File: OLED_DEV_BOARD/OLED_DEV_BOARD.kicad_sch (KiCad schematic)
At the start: 1 part

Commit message: Added some parts
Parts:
- added U?: NCP1117-3.3_TO252, Package_TO_SOT_SMD:TO-252-2, symbol Regulator_Linear:NCP1117-3.3_TO252
- added U?: IS66WVS1M8BLL-104NLI, symbol OLED:IS66WVS1M8BLL-104NLI
- added U?: W25Q32JVSS, Package_SO:SOIC-8_5.23x5.23mm_P1.27mm, symbol Memory_Flash:W25Q32JVSS
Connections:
- net +3V3: now also U?.8 (VCC), U?.8 (VDD)
- net GND: now also U?.4 (GND), U?.4 (VSS)
- new net FLASH_CLK: U?.6 (CLK)
- new net FLASH_CSb: U?.1 (~{CS})
- new net FLASH_D0: U?.5 (DI(IO0))
- new net FLASH_D1: U?.2 (DO(IO1))
- new net FLASH_D2: U?.3 (IO2)
- new net FLASH_D3: U?.7 (IO3)
- new net PSRAM_CLK: U?.6 (CLK)
- new net PSRAM_CSb: U?.1 (CE#)
- new net PSRAM_D0: U?.5 (SI/SIO0)
- new net PSRAM_D1: U?.2 (SO/SIO1)
- new net PSRAM_D2: U?.3 (SIO2)
- new net PSRAM_D3: U?.7 (SIO3)

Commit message: Added switches
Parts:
- added C?: 100uF, symbol Device:C_Polarized
- added C? (x2): 10uF, symbol Device:C_Polarized
- added C? (x2): 100nF, symbol Device:C
- added C? (x2): 1uF, symbol Device:C
- added C?: 1nF, symbol Device:C
- added D?: 1N4004, Diode_THT:D_DO-41_SOD81_P10.16mm_Horizontal, symbol Diode:1N4004
- added J?: Conn_02x20_Odd_Even, symbol Connector_Generic:Conn_02x20_Odd_Even
- added J?: AudioJack3_Ground, Connector_Audio:Jack_3.5mm_CUI_SJ-3523-SMT_Horizontal, symbol Connector:AudioJack3_Ground
- added J?: Barrel_Jack, symbol Connector:Barrel_Jack
- added R? (x9): 5k6, symbol Device:R
- added SW? (x6): SW_MEC_5E, symbol Switch:SW_MEC_5E
- added SW?: SW_DIP_x02, symbol Switch:SW_DIP_x02
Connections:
- net +3V3: now also U?.2 (VO), C?.1, C?.1, C?.1, C?.1, C?.1, C?.1, D?.2 (A), SW?.3, SW?.3 (K), SW?.3 (K), SW?.3 (K), SW?.3 (K), SW?.3 (K), SW?.3 (K), SW?.4, SW?.4 (A), SW?.4 (A), SW?.4 (A), SW?.4 (A), SW?.4 (A), SW?.4 (A)
- net GND: now also U?.1 (GND), C?.2, C?.2, C?.2, C?.2, C?.2, C?.2, C?.2, C?.2, J?.1 (Pin_1), J?.2, J?.2 (Pin_2), J?.39 (Pin_39), J?.40 (Pin_40), J?.G, J?.S, R?.1, R?.1, R?.1, R?.1, R?.1, R?.1, R?.1, R?.2
- net at U?.3 (VI): now also C?.1, D?.1 (K), J?.1
- new net: R?.2, SW?.1, SW?.2 (x5)
- new net: R?.1, SW?.1, SW?.2
- new net: C?.1, J?.R, J?.T, R?.2
- new net: R?.2, SW?.1
- new net: R?.2, SW?.2
- new net PWM: R?.1
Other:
- moved on the sheet: U?

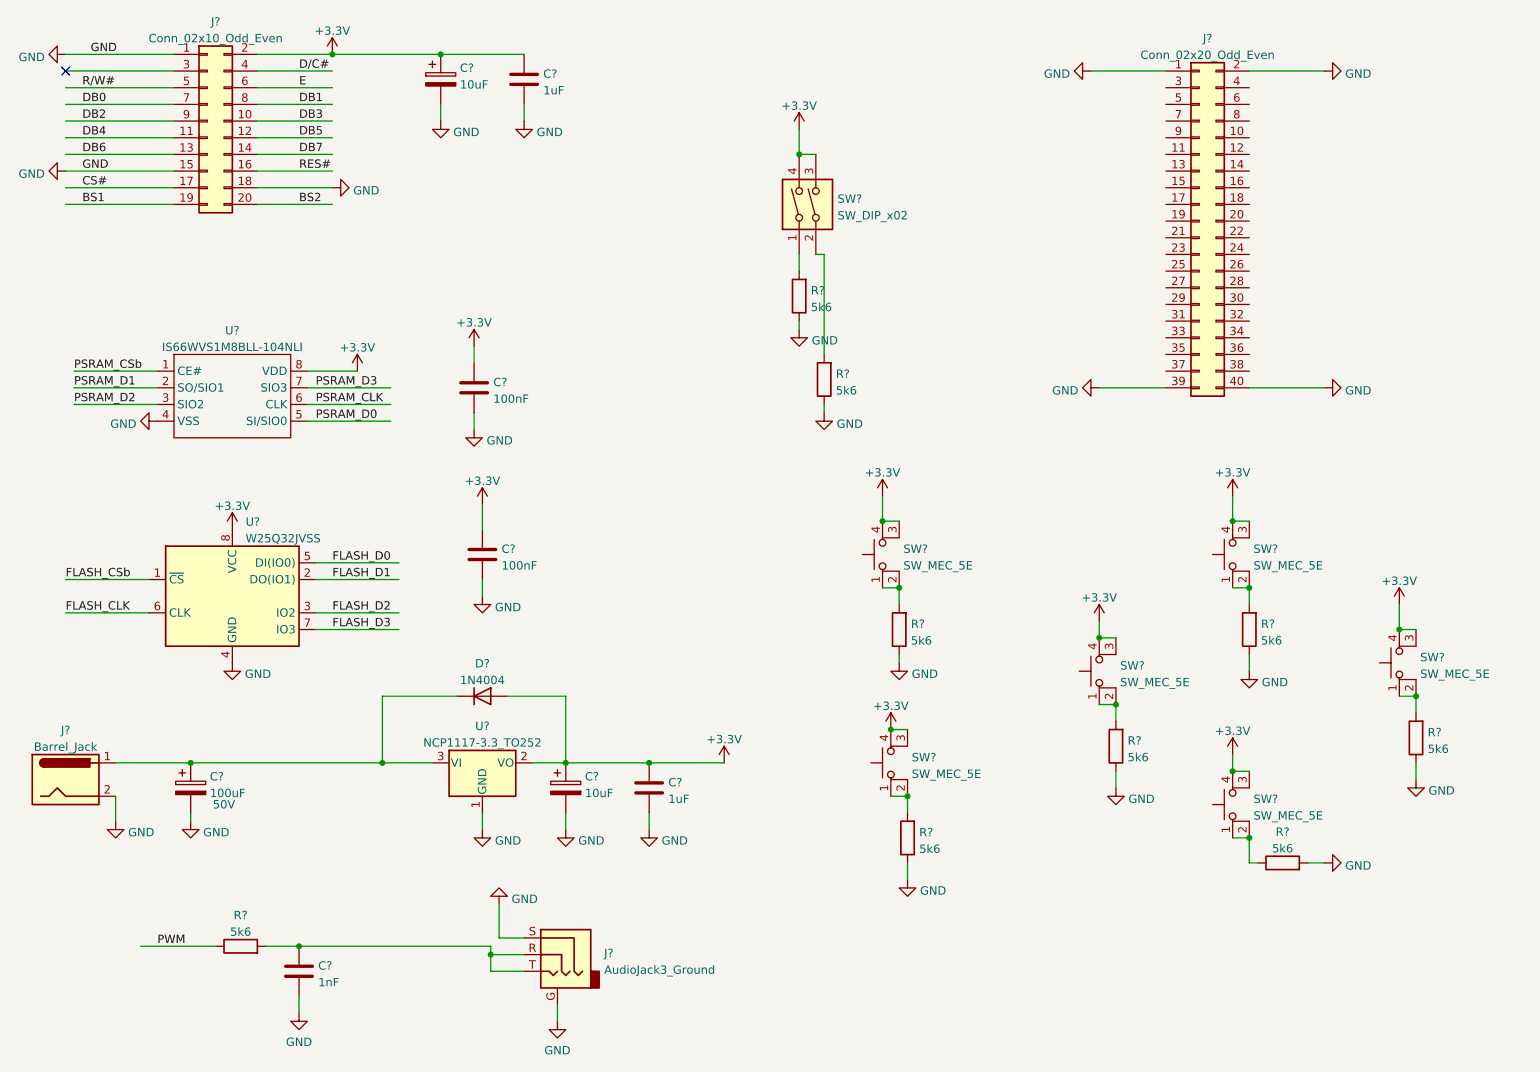
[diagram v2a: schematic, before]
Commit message: Added signals to connector
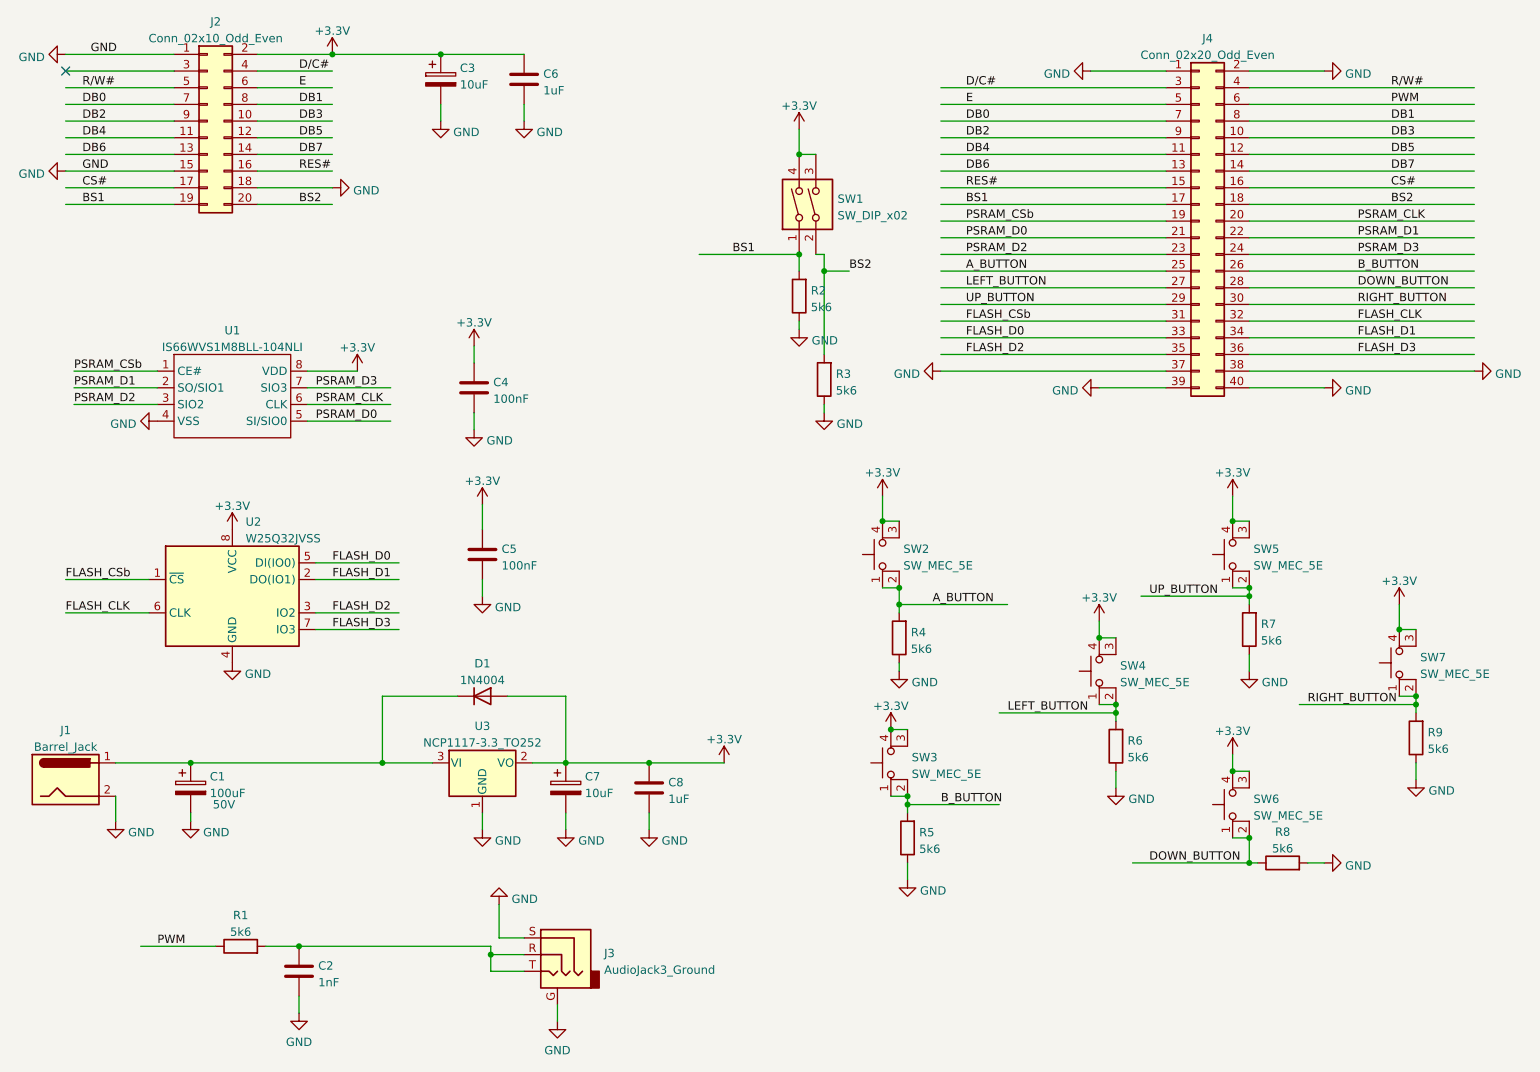
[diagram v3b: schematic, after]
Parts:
- gave numbers to parts that had none: 32
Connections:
- net BS1: now also J4.17 (Pin_17), R2.2, SW1.1
- net BS2: now also J4.18 (Pin_18), R3.2, SW1.2
- net CS#: now also J4.16 (Pin_16)
- net DB0: now also J4.7 (Pin_7)
- net DB1: now also J4.8 (Pin_8)
- net DB2: now also J4.9 (Pin_9)
- net DB3: now also J4.10 (Pin_10)
- net DB4: now also J4.11 (Pin_11)
- net DB5: now also J4.12 (Pin_12)
- net DB6: now also J4.13 (Pin_13)
- net DB7: now also J4.14 (Pin_14)
- net D/C#: now also J4.3 (Pin_3)
- net E: now also J4.5 (Pin_5)
- net FLASH_CLK: now also J4.32 (Pin_32)
- net FLASH_CSb: now also J4.31 (Pin_31)
- net FLASH_D0: now also J4.33 (Pin_33)
- net FLASH_D1: now also J4.34 (Pin_34)
- net FLASH_D2: now also J4.35 (Pin_35)
- net FLASH_D3: now also J4.36 (Pin_36)
- net GND: now also J4.37 (Pin_37), J4.38 (Pin_38)
- net PSRAM_CLK: now also J4.20 (Pin_20)
- net PSRAM_CSb: now also J4.19 (Pin_19)
- net PSRAM_D0: now also J4.21 (Pin_21)
- net PSRAM_D1: now also J4.22 (Pin_22)
- net PSRAM_D2: now also J4.23 (Pin_23)
- net PSRAM_D3: now also J4.24 (Pin_24)
- net PWM: now also J4.6 (Pin_6)
- net RES#: now also J4.15 (Pin_15)
- net R/W#: now also J4.4 (Pin_4)
- net B_BUTTON: now reaches R5.2, SW3.1, SW3.2
- net B_BUTTON: now also J4.26 (Pin_26)
- net RIGHT_BUTTON: now reaches R9.2, SW7.1, SW7.2
- net RIGHT_BUTTON: now also J4.30 (Pin_30)
- net UP_BUTTON: now reaches R7.2, SW5.1, SW5.2
- net UP_BUTTON: now also J4.29 (Pin_29)
- net LEFT_BUTTON: now reaches R6.2, SW4.1, SW4.2
- net LEFT_BUTTON: now also J4.27 (Pin_27)
- net A_BUTTON: now reaches J4.25 (Pin_25)
- net A_BUTTON: now also R4.2, SW2.1, SW2.2
- net DOWN_BUTTON: now reaches J4.28 (Pin_28)
- net DOWN_BUTTON: now also R8.1, SW6.1, SW6.2
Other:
- moved on the sheet: R4

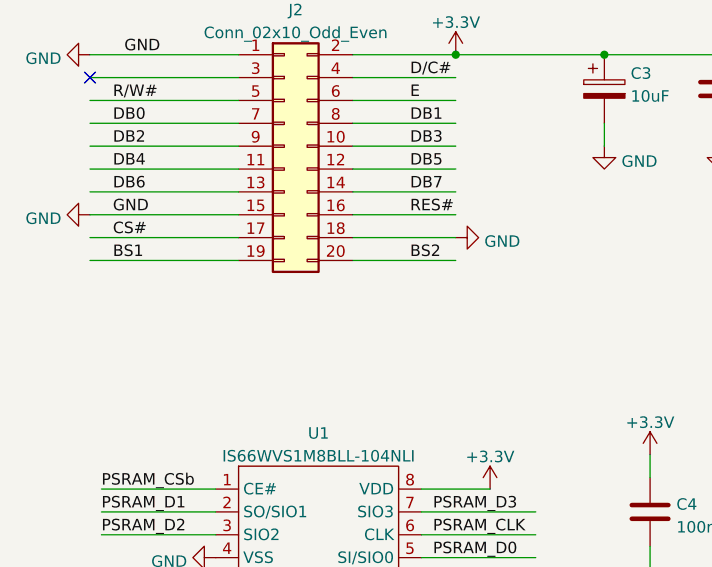
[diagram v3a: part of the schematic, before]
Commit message: Added part number to header
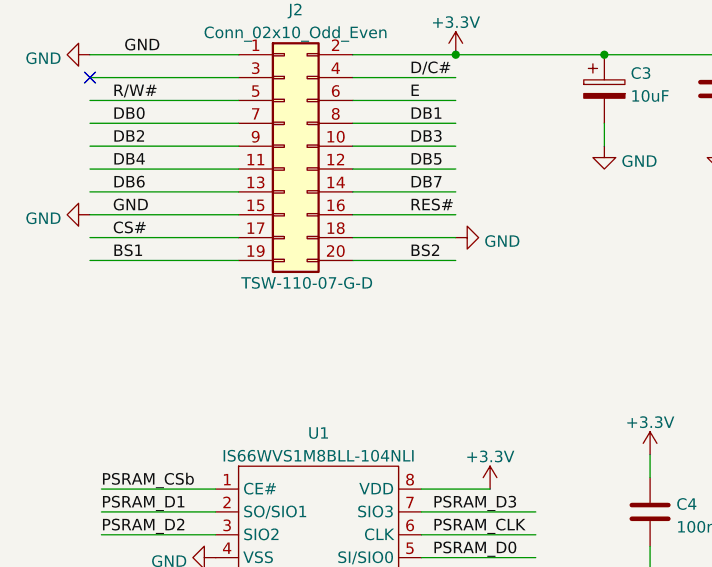
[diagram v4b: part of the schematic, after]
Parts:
- J2: Manufacturer Part Number (none) -> TSW-110-07-G-D; Mouser Part Number (none) -> 200-TSW11007GD
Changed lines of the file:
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@@
   )
   (symbol (lib_id "Connector_Generic:Conn_02x10_Odd_Even") (at 48.26 45.72 0) (unit 1)
-    (in_bom yes) (on_board yes) (fields_autoplaced)
+    (in_bom yes) (on_board yes)
     (property "Reference" "J2" (id 0) (at 49.53 30.5902 0))
     (property "Value" "Conn_02x10_Odd_Even" (id 1) (at 49.53 33.1271 0))
@@
       (effects (font (size 1.27 1.27)) hide)
     )
+    (property "Mouser Part Number" "200-TSW11007GD " (id 4) (at 48.26 45.72 0)
+      (effects (font (size 1.27 1.27)) hide)
+    )
+    (property "Manufacturer Part Number" "TSW-110-07-G-D " (id 5) (at 50.8 60.96 0))
     (pin "1")
     (pin "10")

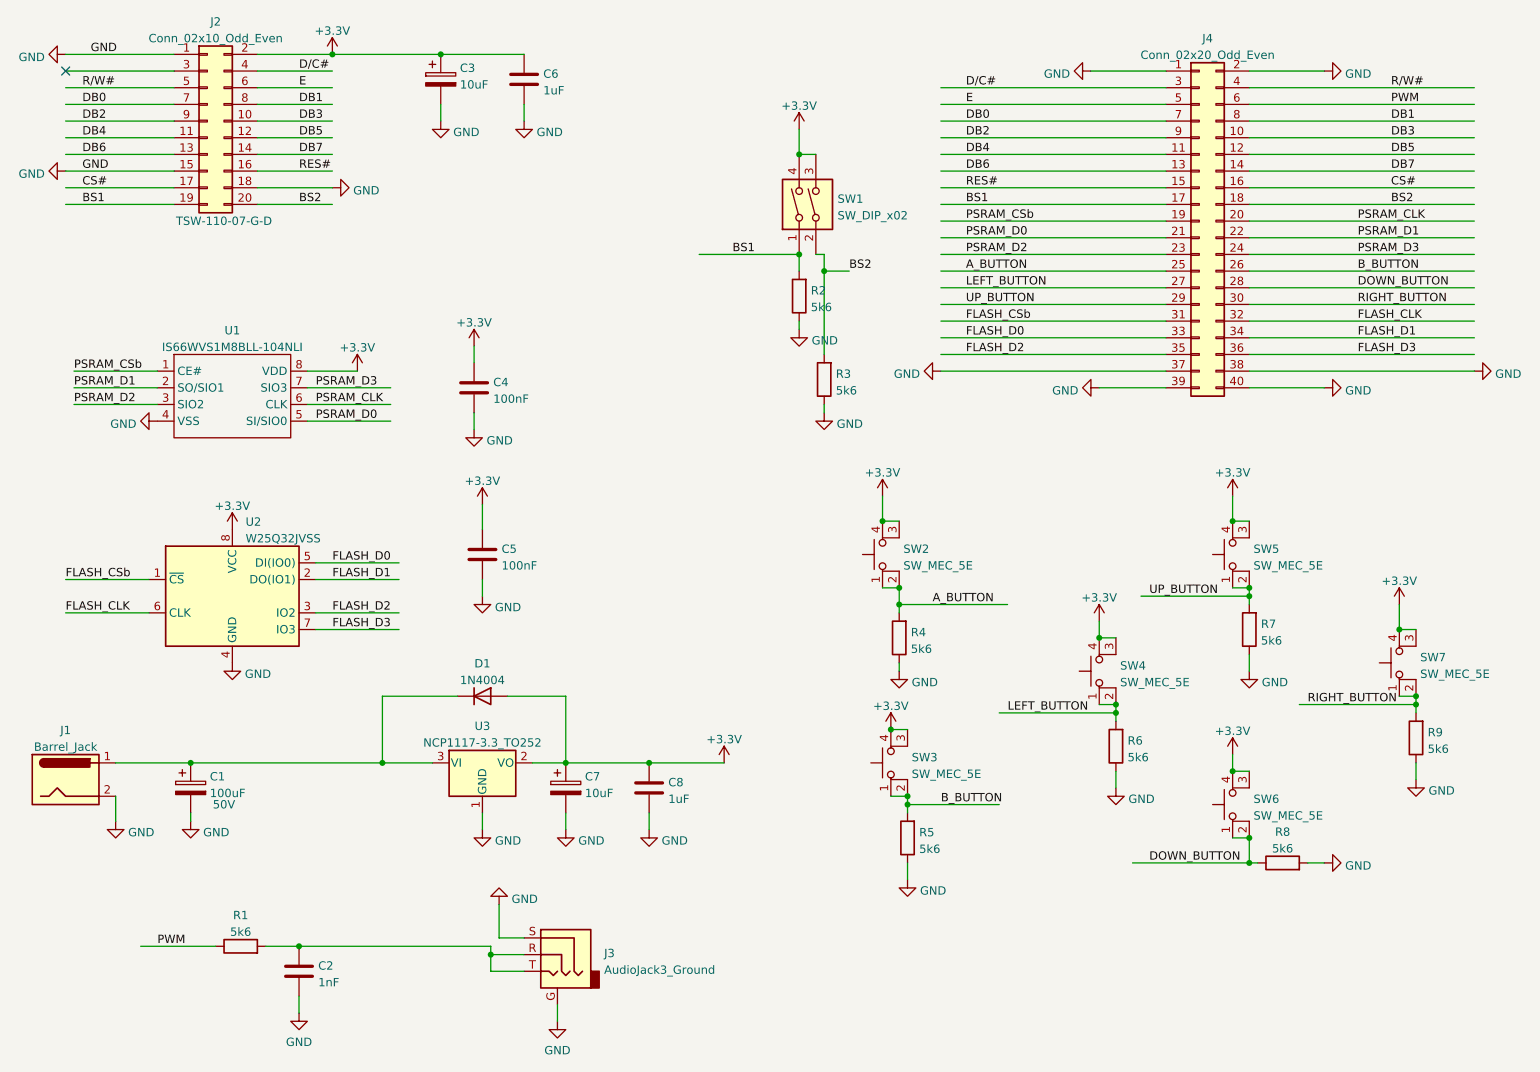
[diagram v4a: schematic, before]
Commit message: Added part numbers and footprints
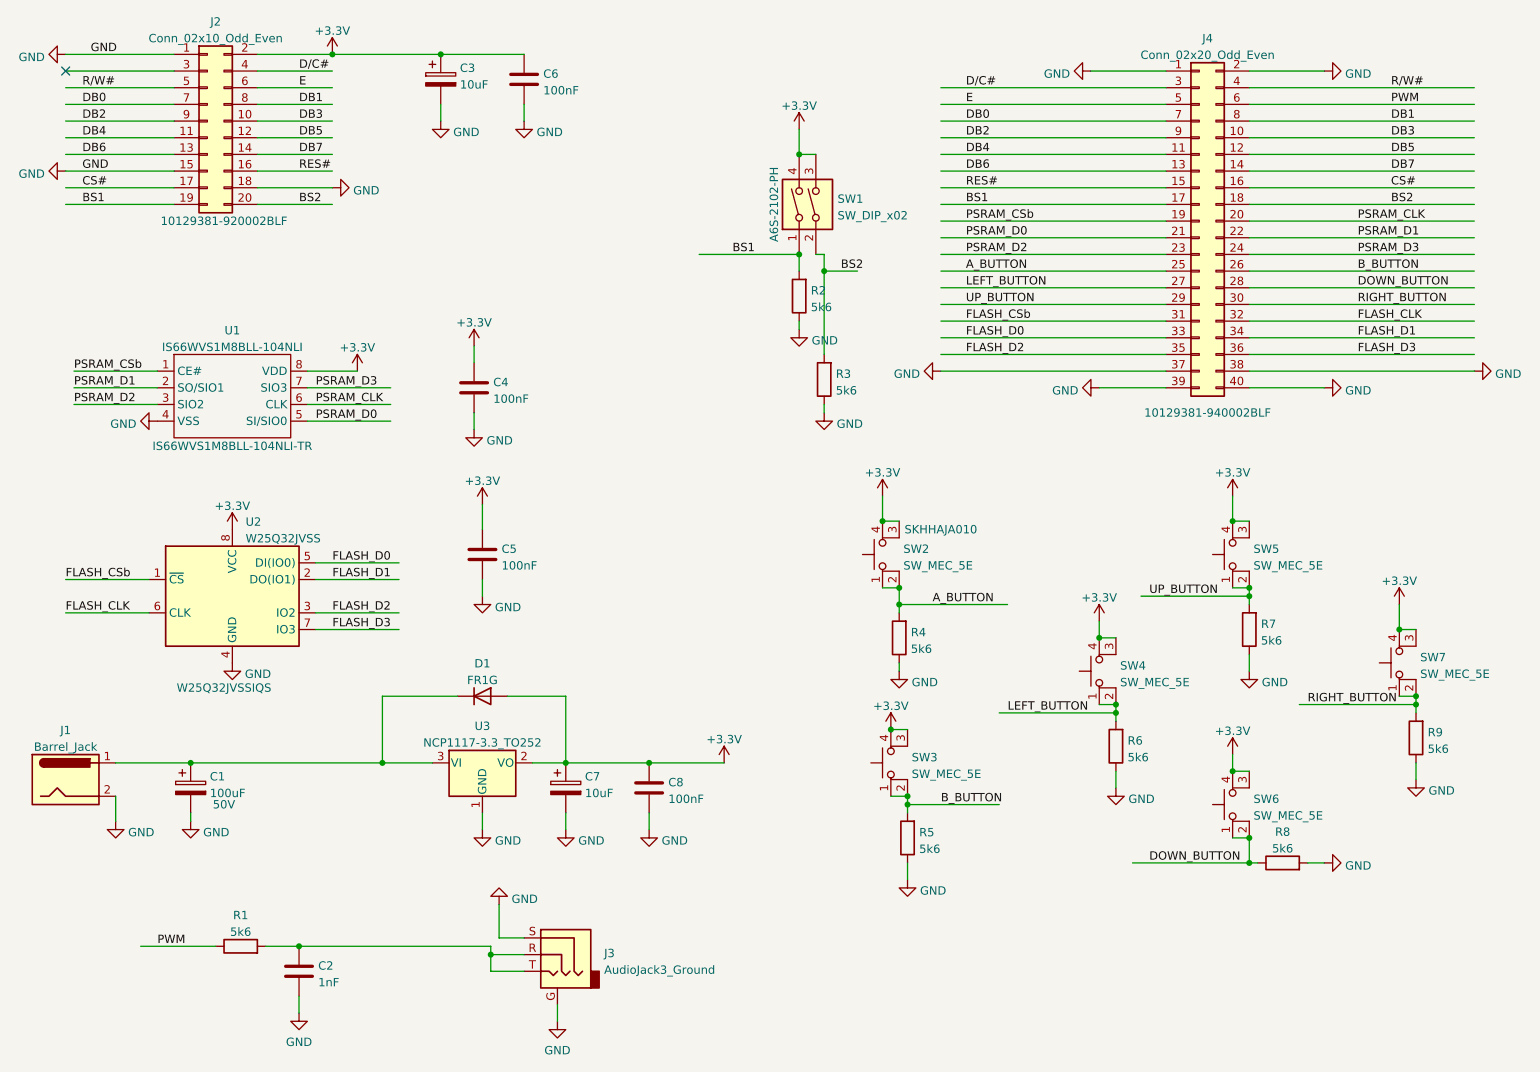
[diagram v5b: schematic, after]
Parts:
- C1: footprint (none) -> Capacitor_SMD:CP_Elec_10x10; Manufacturer Part Number (none) -> GXC1H101MCQ1GS; Mouser Part Number (none) -> 647-GXC1H101MCQ1GS
- C2: footprint (none) -> Capacitor_SMD:C_0603_1608Metric; Manufacturer Part Number (none) -> C0603C102K4RAC7411; Mouser Part Number (none) -> 80-C0603C102K4RACLR
- C3, C7: footprint (none) -> Capacitor_SMD:C_1206_3216Metric; Manufacturer Part Number (none) -> CL31B106KQHNFNE; Mouser Part Number (none) -> 187-CL31B106KQHNFNE
- C4, C5: footprint (none) -> Capacitor_SMD:C_0603_1608Metric; Manufacturer Part Number (none) -> C0603C104K4RACTU; Mouser Part Number (none) -> 80-C0603C104K4R
- C6, C8: value 1uF -> 100nF; footprint (none) -> Capacitor_SMD:C_0603_1608Metric; Manufacturer Part Number (none) -> C0603C104K4RACTU; Mouser Part Number (none) -> 80-C0603C104K4R
- D1: value 1N4004 -> FR1G; footprint Diode_THT:D_DO-41_SOD81_P10.16mm_Horizontal -> Diode_SMD:D_SMA; Manufacturer Part Number (none) -> FR1G; Mouser Part Number (none) -> 637-FR1G
- J1: footprint (none) -> Connector_BarrelJack:BarrelJack_CUI_PJ-102AH_Horizontal; Manufacturer Part Number (none) -> PJ-102AH; Mouser Part Number (none) -> 490-PJ-102AH
- J2: footprint (none) -> Connector_PinHeader_2.54mm:PinHeader_2x10_P2.54mm_Vertical; Manufacturer Part Number TSW-110-07-G-D -> 10129381-920002BLF; Mouser Part Number 200-TSW11007GD -> 649-1012938192002BLF
- J3: Manufacturer Part Number (none) -> SJ-3523-SMT-TR; Mouser Part Number (none) -> 490-SJ-3523-SMT-TR
- J4: footprint (none) -> Connector_PinHeader_2.54mm:PinHeader_2x20_P2.54mm_Vertical; Manufacturer Part Number (none) -> 10129381-940002BLF; Mouser Part Number (none) -> 649-1012938194002BLF
- R1, R2, R3, R4, R5, R6, R7, R8, R9: footprint (none) -> Resistor_SMD:R_0603_1608Metric; Manufacturer Part Number (none) -> AC0603FR-075K6L; Mouser Part Number (none) -> 603-AC0603FR-075K6L
- SW1: footprint (none) -> Button_Switch_SMD:SW_DIP_SPSTx02_Slide_Omron_A6S-210x_W8.9mm_P2.54mm; Manufacturer Part Number (none) -> A6S-2102-PH; Mouser Part Number (none) -> 653-A6S-2102-PH
- SW2, SW3, SW4, SW5, SW6, SW7: footprint (none) -> Button_Switch_THT:SW_Tactile_Straight_KSA0Axx1LFTR; Manufacturer Part Number (none) -> SKHHAJA010; Mouser Part Number (none) -> 688-SKHHAJ
- U1: footprint (none) -> Package_SO:SOIC-8_5.23x5.23mm_P1.27mm; Manufacturer Part Number (none) -> IS66WVS1M8BLL-104NLI-TR; Mouser Part Number (none) -> 870-WVS1M8BLL104NLIT
- U2: Manufacturer Part Number (none) -> W25Q32JVSSIQS; Mouser Part Number (none) -> 454-W25Q32JVSSIQS
- U3: Manufacturer Part Number (none) -> NCP1117DT33RKG; Mouser Part Number (none) -> 863-NCP1117DT33RKG
